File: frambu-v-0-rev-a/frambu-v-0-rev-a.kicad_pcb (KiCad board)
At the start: 2 copper layers, 50 x 60 mm, 30 parts, among them J3 Conn_02x18_Odd_Even, J4 Conn_02x18_Odd_Even, J5 USB_C_Receptacle_USB2.0_16P, SW1 PTS 636, U1 RP2040, U2 AMS1117-5.0, U3 W25Q128JVS

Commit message: nombre nuevo frambu
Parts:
- C12, C18: footprint frambuesa-rev-a:C1206 -> frambu-v-0-rev-a:C1206
- C13, C19, C20: footprint frambuesa-rev-a:C0402 -> frambu-v-0-rev-a:C0402
- J5: footprint frambuesa-rev-a:USB-C_SMD-TYPE-C-31-M-12_1 -> frambu-v-0-rev-a:USB-C_SMD-TYPE-C-31-M-12_1
- R4, R6, R7: footprint frambuesa-rev-a:R0402 -> frambu-v-0-rev-a:R0402
- SW1: footprint frambuesa-rev-a:KEY-SMD_L6.0-W3.5-LS8.7 -> frambu-v-0-rev-a:KEY-SMD_L6.0-W3.5-LS8.7
- U3: footprint frambuesa-rev-a:SOIC-8_L5.3-W5.3-P1.27-LS8.0-BL -> frambu-v-0-rev-a:SOIC-8_L5.3-W5.3-P1.27-LS8.0-BL
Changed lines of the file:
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@@
 		(property ki_fp_filters "C_*")
 		(sheetname "/")
-		(sheetfile "frambuesa-rev-a.kicad_sch")
+		(sheetfile "frambu-v-0-rev-a.kicad_sch")
 		(units
 			(unit
@@
 		(property ki_fp_filters "C_*")
 		(sheetname "/")
-		(sheetfile "frambuesa-rev-a.kicad_sch")
+		(sheetfile "frambu-v-0-rev-a.kicad_sch")
 		(units
 			(unit
@@
 		(property ki_fp_filters "C_*")
 		(sheetname "/")
-		(sheetfile "frambuesa-rev-a.kicad_sch")
+		(sheetfile "frambu-v-0-rev-a.kicad_sch")
 		(units
 			(unit
@@
 		(property ki_fp_filters "Connector*:*_2x??_*")
 		(sheetname "/")
-		(sheetfile "frambuesa-rev-a.kicad_sch")
+		(sheetfile "frambu-v-0-rev-a.kicad_sch")
 		(units
 			(unit
@@
 		(property ki_fp_filters "*QFN*7x7mm?P0.4mm?EP3.2x3.2mm*")
 		(sheetname "/")
-		(sheetfile "frambuesa-rev-a.kicad_sch")
+		(sheetfile "frambu-v-0-rev-a.kicad_sch")
 		(units
 			(unit
@@
 		)
 	)
-	(footprint "frambuesa-rev-a:KEY-SMD_L6.0-W3.5-LS8.7"
+	(footprint "frambu-v-0-rev-a:KEY-SMD_L6.0-W3.5-LS8.7"
 		(layer "F.Cu")
 		(at 82.23 44.935)
@@
 		)
 		(sheetname "/")
-		(sheetfile "frambuesa-rev-a.kicad_sch")
+		(sheetfile "frambu-v-0-rev-a.kicad_sch")
 		(units
 			(unit
@@
 		(property ki_fp_filters "C_*")
 		(sheetname "/")
-		(sheetfile "frambuesa-rev-a.kicad_sch")
+		(sheetfile "frambu-v-0-rev-a.kicad_sch")
 		(units
 			(unit
@@
 		)
 	)
-	(footprint "frambuesa-rev-a:SOIC-8_L5.3-W5.3-P1.27-LS8.0-BL"
+	(footprint "frambu-v-0-rev-a:SOIC-8_L5.3-W5.3-P1.27-LS8.0-BL"
 		(layer "F.Cu")
 		(at 72.15 70.835)
@@
 		(property ki_fp_filters "*SOIC*5.3x5.3mm*P1.27mm*")
 		(sheetname "/")
-		(sheetfile "frambuesa-rev-a.kicad_sch")
+		(sheetfile "frambu-v-0-rev-a.kicad_sch")
 		(units
 			(unit
@@
 		)
 		(embedded_fonts no)
-		(model "bibliotecas/frambuesa-rev-a.3dshapes/SOIC-8_L5.3-W5.3-H1.9-LS7.9-P1.27.wrl"
+		(model "bibliotecas/frambu-v-0-rev-a.3dshapes/SOIC-8_L5.3-W5.3-H1.9-LS7.9-P1.27.wrl"
 			(offset
 				(xyz 0 0 0)
@@
 		)
 	)
-	(footprint "frambuesa-rev-a:R0402"
+	(footprint "frambu-v-0-rev-a:R0402"
 		(layer "F.Cu")
 		(at 87.045 27.725)
@@
 		(property ki_fp_filters "R_*")
 		(sheetname "/")
-		(sheetfile "frambuesa-rev-a.kicad_sch")
+		(sheetfile "frambu-v-0-rev-a.kicad_sch")
 		(units
 			(unit
@@
 		)
 		(embedded_fonts no)
-		(model "bibliotecas/frambuesa-rev-a.3dshapes/R0402_L1.0-W0.5-H0.4.wrl"
+		(model "bibliotecas/frambu-v-0-rev-a.3dshapes/R0402_L1.0-W0.5-H0.4.wrl"
 			(offset
 				(xyz 0 0 0)
@@
 		)
 	)
-	(footprint "frambuesa-rev-a:C0402"
+	(footprint "frambu-v-0-rev-a:C0402"
 		(layer "F.Cu")
 		(at 86.655 68.905)
@@
 		(property ki_fp_filters "C_*")
 		(sheetname "/")
-		(sheetfile "frambuesa-rev-a.kicad_sch")
+		(sheetfile "frambu-v-0-rev-a.kicad_sch")
 		(units
 			(unit
@@
 		)
 		(embedded_fonts no)
-		(model "bibliotecas/frambuesa-rev-a.3dshapes/C0402_L1.0-W0.5-H0.5.wrl"
+		(model "bibliotecas/frambu-v-0-rev-a.3dshapes/C0402_L1.0-W0.5-H0.5.wrl"
 			(offset
 				(xyz 0 0 0)
@@
 		(property ki_fp_filters "C_*")
 		(sheetname "/")
-		(sheetfile "frambuesa-rev-a.kicad_sch")
+		(sheetfile "frambu-v-0-rev-a.kicad_sch")
 		(units
 			(unit
@@
 		(property ki_fp_filters "C_*")
 		(sheetname "/")
-		(sheetfile "frambuesa-rev-a.kicad_sch")
+		(sheetfile "frambu-v-0-rev-a.kicad_sch")
 		(units
 			(unit
@@
 		)
 	)
-	(footprint "frambuesa-rev-a:R0402"
+	(footprint "frambu-v-0-rev-a:R0402"
 		(layer "F.Cu")
 		(at 87.045 25.575)
@@
 		(property ki_fp_filters "R_*")
 		(sheetname "/")
-		(sheetfile "frambuesa-rev-a.kicad_sch")
+		(sheetfile "frambu-v-0-rev-a.kicad_sch")
 		(units
 			(unit
@@
 		)
 		(embedded_fonts no)
-		(model "bibliotecas/frambuesa-rev-a.3dshapes/R0402_L1.0-W0.5-H0.4.wrl"
+		(model "bibliotecas/frambu-v-0-rev-a.3dshapes/R0402_L1.0-W0.5-H0.4.wrl"
 			(offset
 				(xyz 0 0 0)
@@
 		)
 	)
-	(footprint "frambuesa-rev-a:C0402"
+	(footprint "frambu-v-0-rev-a:C0402"
 		(layer "F.Cu")
 		(at 86.655 66.755)
@@
 		(property ki_fp_filters "C_*")
 		(sheetname "/")
-		(sheetfile "frambuesa-rev-a.kicad_sch")
+		(sheetfile "frambu-v-0-rev-a.kicad_sch")
 		(units
 			(unit
@@
 		)
 		(embedded_fonts no)
-		(model "bibliotecas/frambuesa-rev-a.3dshapes/C0402_L1.0-W0.5-H0.5.wrl"
+		(model "bibliotecas/frambu-v-0-rev-a.3dshapes/C0402_L1.0-W0.5-H0.5.wrl"
 			(offset
 				(xyz 0 0 0)
@@
 		(property ki_fp_filters "C_*")
 		(sheetname "/")
-		(sheetfile "frambuesa-rev-a.kicad_sch")
+		(sheetfile "frambu-v-0-rev-a.kicad_sch")
 		(units
 			(unit
@@
 		(property ki_fp_filters "C_*")
 		(sheetname "/")
-		(sheetfile "frambuesa-rev-a.kicad_sch")
+		(sheetfile "frambu-v-0-rev-a.kicad_sch")
 		(units
 			(unit
@@
 		(property ki_fp_filters "C_*")
 		(sheetname "/")
-		(sheetfile "frambuesa-rev-a.kicad_sch")
+		(sheetfile "frambu-v-0-rev-a.kicad_sch")
 		(units
 			(unit
@@
 		(property ki_fp_filters "SOT?223*TabPin2*")
 		(sheetname "/")
-		(sheetfile "frambuesa-rev-a.kicad_sch")
+		(sheetfile "frambu-v-0-rev-a.kicad_sch")
 		(units
 			(unit
@@
 		(property ki_fp_filters "R_*")
 		(sheetname "/")
-		(sheetfile "frambuesa-rev-a.kicad_sch")
+		(sheetfile "frambu-v-0-rev-a.kicad_sch")
 		(units
 			(unit
@@
 		)
 	)
-	(footprint "frambuesa-rev-a:USB-C_SMD-TYPE-C-31-M-12_1"
+	(footprint "frambu-v-0-rev-a:USB-C_SMD-TYPE-C-31-M-12_1"
 		(layer "F.Cu")
 		(at 74.11 59.970088)
@@
 		(property ki_fp_filters "USB*C*Receptacle*")
 		(sheetname "/")
-		(sheetfile "frambuesa-rev-a.kicad_sch")
+		(sheetfile "frambu-v-0-rev-a.kicad_sch")
 		(units
 			(unit
@@
 		)
 		(embedded_fonts no)
-		(model "bibliotecas/frambuesa-rev-a.3dshapes/USB-C_SMD-TYPE-C-31-M-12_1.wrl"
+		(model "bibliotecas/frambu-v-0-rev-a.3dshapes/USB-C_SMD-TYPE-C-31-M-12_1.wrl"
 			(offset
 				(xyz 0 0 0)
@@
 		(property ki_fp_filters "C_*")
 		(sheetname "/")
-		(sheetfile "frambuesa-rev-a.kicad_sch")
+		(sheetfile "frambu-v-0-rev-a.kicad_sch")
 		(units
 			(unit
@@
 		)
 	)
-	(footprint "frambuesa-rev-a:C1206"
+	(footprint "frambu-v-0-rev-a:C1206"
 		(layer "F.Cu")
 		(at 87.515 52.305)
@@
 		(property ki_fp_filters "C_*")
 		(sheetname "/")
-		(sheetfile "frambuesa-rev-a.kicad_sch")
+		(sheetfile "frambu-v-0-rev-a.kicad_sch")
 		(units
 			(unit
@@
 		)
 		(embedded_fonts no)
-		(model "bibliotecas/frambuesa-rev-a.3dshapes/C1206_L3.2-W1.6-H1.3.wrl"
+		(model "bibliotecas/frambu-v-0-rev-a.3dshapes/C1206_L3.2-W1.6-H1.3.wrl"
 			(offset
 				(xyz 0 0 0)
@@
 		(property ki_fp_filters "R_*")
 		(sheetname "/")
-		(sheetfile "frambuesa-rev-a.kicad_sch")
+		(sheetfile "frambu-v-0-rev-a.kicad_sch")
 		(units
 			(unit
@@
 		(property ki_fp_filters "C_*")
 		(sheetname "/")
-		(sheetfile "frambuesa-rev-a.kicad_sch")
+		(sheetfile "frambu-v-0-rev-a.kicad_sch")
 		(units
 			(unit
@@
 		)
 	)
-	(footprint "frambuesa-rev-a:R0402"
+	(footprint "frambu-v-0-rev-a:R0402"
 		(layer "F.Cu")
 		(at 87.045 29.875)
@@
 		(property ki_fp_filters "R_*")
 		(sheetname "/")
-		(sheetfile "frambuesa-rev-a.kicad_sch")
+		(sheetfile "frambu-v-0-rev-a.kicad_sch")
 		(units
 			(unit
@@
 		)
 		(embedded_fonts no)
-		(model "bibliotecas/frambuesa-rev-a.3dshapes/R0402_L1.0-W0.5-H0.4.wrl"
+		(model "bibliotecas/frambu-v-0-rev-a.3dshapes/R0402_L1.0-W0.5-H0.4.wrl"
 			(offset
 				(xyz 0 0 0)
@@
 		(property ki_fp_filters "C_*")
 		(sheetname "/")
-		(sheetfile "frambuesa-rev-a.kicad_sch")
+		(sheetfile "frambu-v-0-rev-a.kicad_sch")
 		(units
 			(unit
@@
 		)
 	)
-	(footprint "frambuesa-rev-a:C0402"
+	(footprint "frambu-v-0-rev-a:C0402"
 		(layer "F.Cu")
 		(at 86.655 71.055)
@@
 		(property ki_fp_filters "C_*")
 		(sheetname "/")
-		(sheetfile "frambuesa-rev-a.kicad_sch")
+		(sheetfile "frambu-v-0-rev-a.kicad_sch")
 		(units
 			(unit
@@
 		)
 		(embedded_fonts no)
-		(model "bibliotecas/frambuesa-rev-a.3dshapes/C0402_L1.0-W0.5-H0.5.wrl"
+		(model "bibliotecas/frambu-v-0-rev-a.3dshapes/C0402_L1.0-W0.5-H0.5.wrl"
 			(offset
 				(xyz 0 0 0)
@@
 		(property ki_fp_filters "Connector*:*_2x??_*")
 		(sheetname "/")
-		(sheetfile "frambuesa-rev-a.kicad_sch")
+		(sheetfile "frambu-v-0-rev-a.kicad_sch")
 		(units
 			(unit
@@
 		)
 	)
-	(footprint "frambuesa-rev-a:C1206"
+	(footprint "frambu-v-0-rev-a:C1206"
 		(layer "F.Cu")
 		(at 87.515 48.975)
@@
 		(property ki_fp_filters "C_*")
 		(sheetname "/")
-		(sheetfile "frambuesa-rev-a.kicad_sch")
+		(sheetfile "frambu-v-0-rev-a.kicad_sch")
 		(units
 			(unit
@@
 		)
 		(embedded_fonts no)
-		(model "bibliotecas/frambuesa-rev-a.3dshapes/C1206_L3.2-W1.6-H1.3.wrl"
+		(model "bibliotecas/frambu-v-0-rev-a.3dshapes/C1206_L3.2-W1.6-H1.3.wrl"
 			(offset
 				(xyz 0 0 0)
@@
 		(property ki_fp_filters "MountingHole*")
 		(sheetname "/")
-		(sheetfile "frambuesa-rev-a.kicad_sch")
+		(sheetfile "frambu-v-0-rev-a.kicad_sch")
 		(units
 			(unit

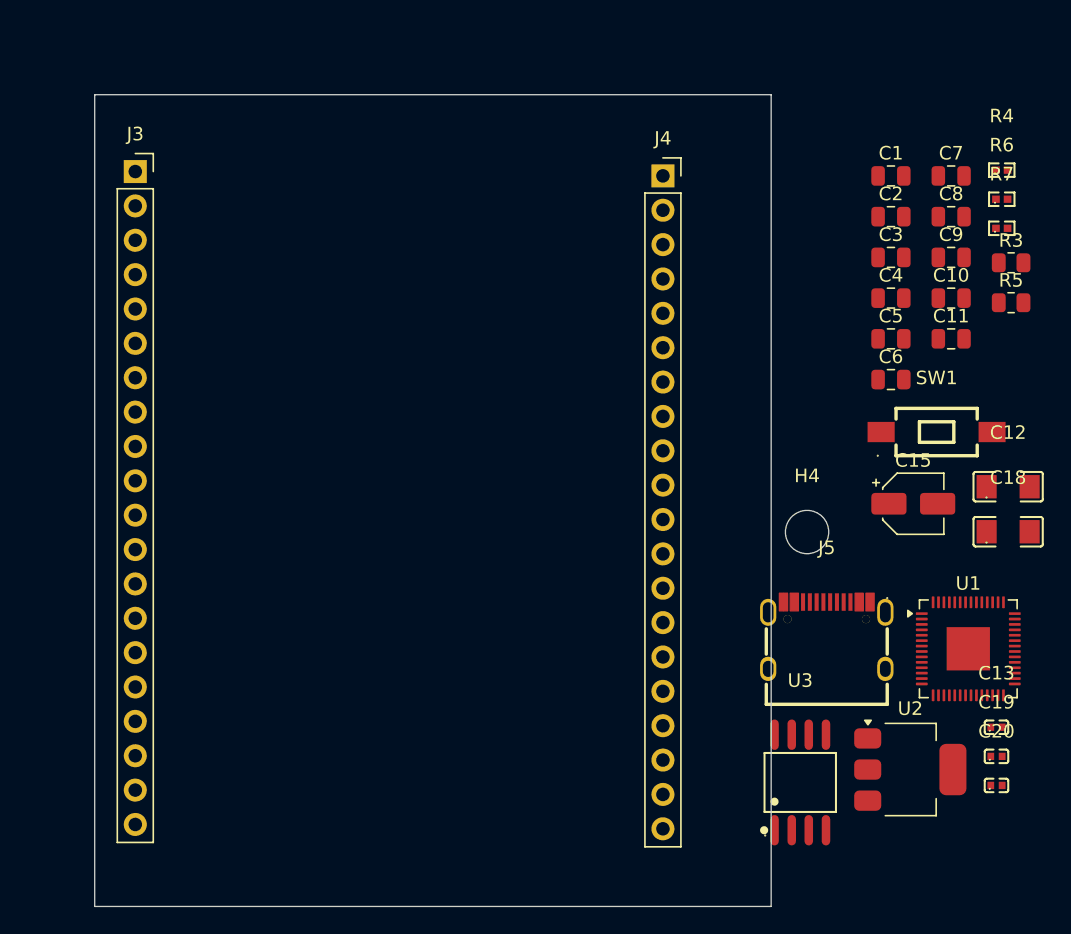
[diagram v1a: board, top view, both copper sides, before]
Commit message: agregar version de pcb
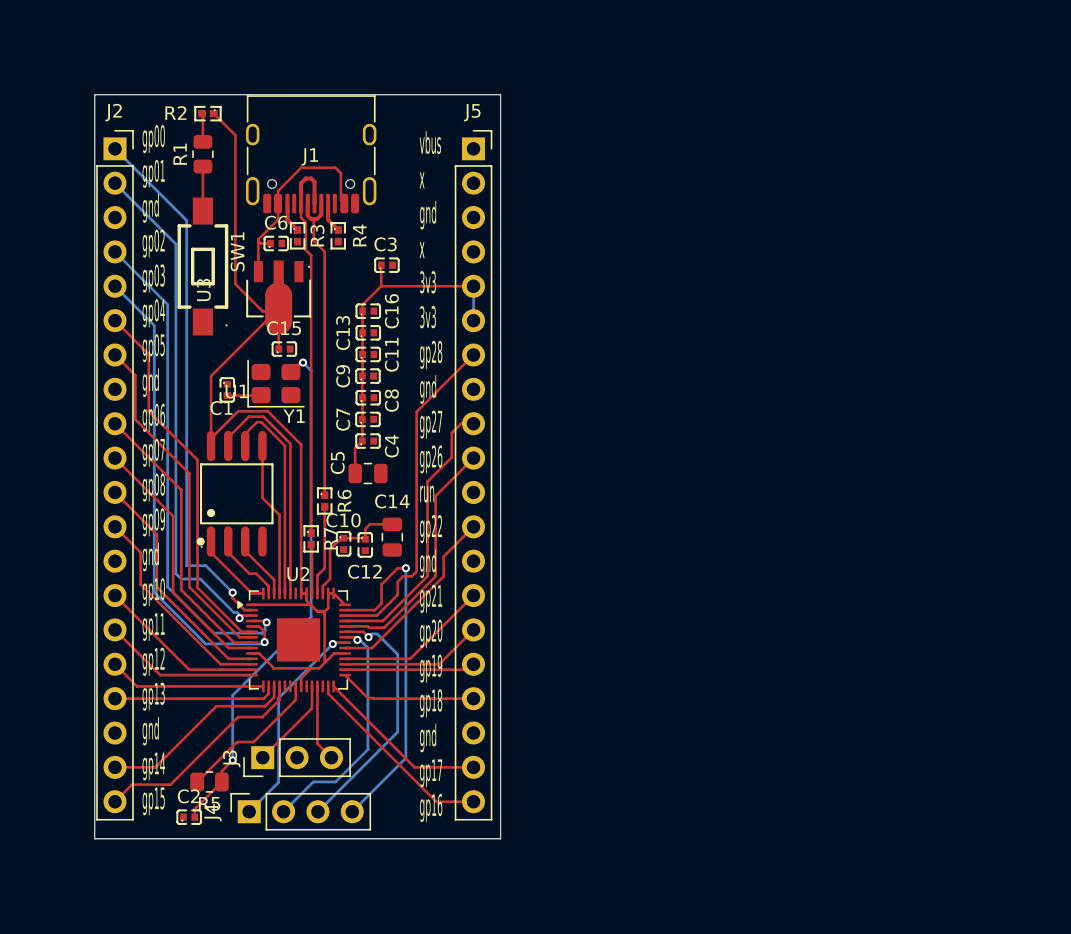
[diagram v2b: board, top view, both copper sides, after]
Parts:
- removed C18: 100u, frambu-v-0-rev-a:C1206
- removed C19, C20: 10u, frambu-v-0-rev-a:C0402
- removed H4: MountingHole, MountingHole:MountingHole_3.2mm_M3
- added C14: 1u, Capacitor_SMD:C_0805_2012Metric, F.Cu at (42.0, 52.7)
- added C16: 100n, frambu-v-0-rev-a:C0402, F.Cu at (40.2, 36.0)
- added J1: USB_C_Receptacle_USB2.0_16P, Connector_USB:USB_C_Receptacle_HRO_TYPE-C-31-M-12, F.Cu at (36.0, 24.0)
- added J2: pico_pines_1-20, Connector_PinSocket_2.54mm:PinSocket_1x20_P2.54mm_Vertical, F.Cu at (21.5, 24.0)
- added R1: 1k, Resistor_SMD:R_0805_2012Metric, F.Cu at (28.0, 24.4)
- added R2: 10k, frambu-v-0-rev-a:R0402, F.Cu at (28.4, 21.4)
- added Y1: 12MHz, Crystal:Crystal_SMD_3225-4Pin_3.2x2.5mm, F.Cu at (33.4, 41.4)
- C1: value 1u -> 15p; footprint Capacitor_SMD:C_0805_2012Metric -> frambu-v-0-rev-a:C0402
- C10, C11, C4, C7, C8: footprint Capacitor_SMD:C_0805_2012Metric -> frambu-v-0-rev-a:C0402
- C12: value 100u -> 100n; footprint frambu-v-0-rev-a:C1206 -> frambu-v-0-rev-a:C0402
- C13: value 10u -> 100n
- C15: footprint Capacitor_SMD:CP_Elec_4x5.4 -> frambu-v-0-rev-a:C0402
- C2: value 100n -> 15p; footprint Capacitor_SMD:C_0805_2012Metric -> frambu-v-0-rev-a:C0402
- C3, C6: value 100n -> 10u; footprint Capacitor_SMD:C_0805_2012Metric -> frambu-v-0-rev-a:C0402
- C5: value 100n -> 1u
- C9: value 1u -> 100n; footprint Capacitor_SMD:C_0805_2012Metric -> frambu-v-0-rev-a:C0402
- J3: value Conn_02x18_Odd_Even -> SWD; footprint Connector_PinSocket_2.54mm:PinSocket_1x20_P2.54mm_Vertical -> Connector_PinHeader_2.54mm:PinHeader_1x03_P2.54mm_Vertical
- J4: value Conn_02x18_Odd_Even -> GPIO_extra; footprint Connector_PinSocket_2.54mm:PinSocket_1x20_P2.54mm_Vertical -> Connector_PinSocket_2.54mm:PinSocket_1x04_P2.54mm_Vertical
- J5: value USB_C_Receptacle_USB2.0_16P -> pico_pines_40-21; footprint frambu-v-0-rev-a:USB-C_SMD-TYPE-C-31-M-12_1 -> Connector_PinSocket_2.54mm:PinSocket_1x20_P2.54mm_Vertical
- R3: value 1k -> 5k1; footprint Resistor_SMD:R_0805_2012Metric -> frambu-v-0-rev-a:R0402
- R4: value 10k -> 5k1
- R5: value 1K -> 1k
- R6, R7: value 5k1 -> 27
- U1: value RP2040 -> W25Q128JVS; footprint Package_DFN_QFN:QFN-56-1EP_7x7mm_P0.4mm_EP3.2x3.2mm -> frambu-v-0-rev-a:SOIC-8_L5.3-W5.3-P1.27-LS8.0-BL
- U2: value AMS1117-5.0 -> RP2040; footprint Package_TO_SOT_SMD:SOT-223-3_TabPin2 -> Package_DFN_QFN:QFN-56-1EP_7x7mm_P0.4mm_EP3.2x3.2mm
- U3: value W25Q128JVS -> AMS1117-3.3; footprint frambu-v-0-rev-a:SOIC-8_L5.3-W5.3-P1.27-LS8.0-BL -> frambu-v-0-rev-a:SOT-89-3_L4.5-W2.5-P1.50-LS4.2-BR
- moved R5 69.0 mm to (28.5, 70.8), turned to 180 degrees
- moved C2 68.3 mm to (27.0, 73.4)
- moved J4 56.1 mm to (31.4, 73.0), turned to 90 degrees
- moved R7 56.0 mm to (36.0, 52.8), turned to -90 degrees
- moved SW1 55.6 mm to (28.0, 32.7), turned to 90 degrees
- moved U1 55.3 mm to (30.5, 49.5)
- moved C13 54.8 mm to (40.2, 37.6)
- moved R6 54.8 mm to (37.0, 50.0), turned to -90 degrees
- moved U3 53.0 mm to (33.6, 34.4), turned to 90 degrees
- moved R3 52.8 mm to (35.0, 30.4), turned to -90 degrees
- moved C1 51.5 mm to (29.8, 41.8), turned to -90 degrees
- moved R4 49.3 mm to (38.0, 30.4), turned to -90 degrees
- moved C10 48.4 mm to (38.4, 53.2), turned to -90 degrees
- moved C15 47.9 mm to (34.0, 38.8)
- moved C12 47.7 mm to (40.0, 53.3), turned to -90 degrees
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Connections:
- C1 pad 1: +3V3 -> GND
- C1 pad 2: GND -> /XIN
- C11 pad 1: +1V1 -> +3V3
- C12 pad 1: VHI -> +1V1
- C13 pad 1: VHI -> +3V3
- C2 pad 1: +3V3 -> GND
- C2 pad 2: GND -> Net-(C2-Pad2)
- C6 pad 1: +3V3 -> VBUS
- C9 pad 1: +1V1 -> +3V3
- J3 pad 1: GND -> /SWCLK
- J3 pad 2: +3V3 -> GND
- J3 pad 3: GND -> /SWD
- J4 pad 1: /GPIO29_ADC3 -> /GPIO23
- J4 pad 2: GND -> /GPIO24
- J4 pad 3: /GPIO28_ADC2 -> /GPIO25
- J4 pad 4: GND -> /GPIO29_ADC3
- J5 pad 1: (no net) -> VBUS
- J5 pad 2: (no net) -> unconnected-(J5-Pin_2-Pad2)
- J5 pad 3: (no net) -> GND
- J5 pad 4: (no net) -> unconnected-(J5-Pin_4-Pad4)
- R3 pad 1: Net-(SW1-B) -> Net-(J1-CC2)
- R3 pad 2: /QSPI_SS -> GND
- R4 pad 1: +3V3 -> Net-(J1-CC1)
- R4 pad 2: /QSPI_SS -> GND
- R5 pad 1: Net-(C17-Pad2) -> Net-(C2-Pad2)
- R6 pad 1: Net-(J5-CC1) -> /USB_D-
- R6 pad 2: GND -> Net-(U2-USB_DM)
- R7 pad 1: Net-(J5-CC2) -> /USB_D+
- R7 pad 2: GND -> Net-(U2-USB_DP)
- U1 pad 1: +3V3 -> /QSPI_SS
- U1 pad 2: /GPIO00 -> /QSPI_SD1
- U1 pad 3: /GPIO01 -> /QSPI_SD2
- U1 pad 4: /GPIO02 -> GND
- U1 pad 5: /GPIO03 -> /QSPI_SD0
- U1 pad 6: /GPIO04 -> /QSPI_SCLK
- U1 pad 7: /GPIO05 -> /QSPI_SD3
- U1 pad 8: /GPIO06 -> +3V3
- U2 pad 1: GND -> +3V3
- U2 pad 2: +3.3V -> /GPIO00
- U2 pad 3: VHI -> /GPIO01
- U3 pad 1: /QSPI_SS -> GND
- U3 pad 2: /QSPI_SD1 -> +3V3
- U3 pad 3: /QSPI_SD2 -> VBUS
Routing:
- net +3V3: track 0.00 -> 102.0 mm
- net /GPIO00: track 0.00 -> 39.4 mm, vias 0 -> 1
- net Net-(C2-Pad2): track 0.00 -> 38.7 mm, vias 0 -> 2
- net /GPIO01: track 0.00 -> 38.0 mm, vias 0 -> 1
- net /GPIO02: track 0.00 -> 36.9 mm, vias 0 -> 1
- net /GPIO03: track 0.00 -> 35.5 mm, vias 0 -> 1
- net /USB_D+: track 0.00 -> 29.0 mm
- net /GPIO04: track 0.00 -> 27.6 mm
- net /GPIO29_ADC3: track 0.00 -> 26.2 mm, vias 0 -> 1
- net /GPIO05: track 0.00 -> 25.6 mm
- net /GPIO28_ADC2: track 0.00 -> 25.0 mm
- net /USB_D-: track 0.00 -> 23.7 mm
- net /GPIO06: track 0.00 -> 21.2 mm
- net /GPIO27_ADC1: track 0.00 -> 20.7 mm
- net /GPIO07: track 0.00 -> 19.2 mm
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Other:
- board size 50 x 60 mm -> 30 x 55 mm
- board text added: "gp00 gp01 gnd gp02 gp03 gp04 gp05 gnd gp06 gp07 gp08 gp09 gnd gp10 gp11 gp12 gp13 gnd gp14 gp15"
- board text added: "vbus x gnd x 3v3 3v3 gp28 gnd gp27 gp26 run gp22 gnd gp21 gp20 gp19 gp18 gnd gp17 gp16"

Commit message: agregar pcb
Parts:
- removed C16, C4, C7, C8: 100n, frambu-v-0-rev-a:C0402
- removed J3: SWD, Connector_PinHeader_2.54mm:PinHeader_1x03_P2.54mm_Vertical
- removed J4: GPIO_extra, Connector_PinSocket_2.54mm:PinSocket_1x04_P2.54mm_Vertical
- moved C13 19.8 mm to (50.5, 54.5)
- moved R5 18.3 mm to (41.8, 58.2), turned to 90 degrees
- moved Y1 18.1 mm to (38.5, 58.8), turned to 180 degrees
- moved C1 17.9 mm to (35.8, 58.8), turned to 90 degrees
- moved R7 17.3 mm to (43.2, 37.1)
- moved R6 17.2 mm to (43.2, 34.0)
- moved R2 17.1 mm to (29.8, 38.4), turned to 90 degrees
- moved C2 16.2 mm to (39.0, 62.5), turned to 180 degrees
- moved U3 15.1 mm to (48.2, 31.0)
- moved C3 14.4 mm to (46.2, 46.2)
- moved C6 13.9 mm to (46.8, 26.9), turned to 90 degrees
- moved C11 12.7 mm to (27.7, 37.0), turned to 90 degrees
- moved U1 11.9 mm to (34.5, 38.2)
- moved C15 11.9 mm to (44.0, 45.2)
- moved U2 11.7 mm to (39.7, 49.5)
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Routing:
- net Net-(C2-Pad2): track 38.7 -> 8.10 mm, vias 2 -> 0
- net GND: track 0.00 -> 29.0 mm, vias 0 -> 3
- net /GPIO29_ADC3: track 26.2 -> 0.00 mm, vias 1 -> 0
- net +1V1: track 9.36 -> 32.9 mm, vias 0 -> 4
- net /QSPI_SS: track 8.04 -> 31.6 mm
- net /RUN: track 0.00 -> 20.8 mm, vias 0 -> 2
- net /GPIO25: track 18.9 -> 0.00 mm, vias 1 -> 0
- net /GPIO24: track 17.8 -> 0.00 mm, vias 1 -> 0
- net VBUS: track 15.4 -> 31.3 mm
- net /GPIO23: track 15.9 -> 0.00 mm, vias 1 -> 0
- net /USB_D-: track 23.7 -> 10.1 mm
- net /GPIO02: track 36.9 -> 23.7 mm, vias 1 -> 0
- net /USB_D+: track 29.0 -> 16.0 mm
- net /GPIO03: track 35.5 -> 22.7 mm, vias 1 -> 0
- net /GPIO16: track 14.6 -> 26.2 mm
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- added copper zone on B.Cu, net GND
- added copper zone on F.Cu, net GND
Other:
- board size 30 x 55 mm -> 40 x 55 mm
- board text added: "2026-10"
- board text added: "frambu"
- board text added: "v-0 rev-a"

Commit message: agregar nueva version frambu
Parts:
- added C4: 100n, frambu-v-0-rev-a:C0402, F.Cu at (52.4, 30.5)
- added C7: 100n, frambu-v-0-rev-a:C0402, F.Cu at (32.2, 46.1)
- added C8: 100n, frambu-v-0-rev-a:C0402, F.Cu at (41.1, 41.5)
- added J3: SWD, Connector_PinHeader_2.54mm:PinHeader_1x03_P2.54mm_Vertical, F.Cu at (37.5, 68.0)
- moved C14 3.00 mm to (40.5, 38.2)
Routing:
- net +1V1: track 32.9 -> 53.1 mm, vias 4 -> 5
- net /SWCLK: track 0.00 -> 18.0 mm, vias 0 -> 2
- net /SWD: track 0.00 -> 15.9 mm, vias 0 -> 2
- net +3V3: track 92.0 -> 103.6 mm
- net /GPIO00: track 29.9 -> 34.1 mm
- net /RUN: track 20.8 -> 21.7 mm
- net /GPIO04: track 19.8 -> 20.7 mm, vias 0 -> 1
- net /GPIO02: track 23.7 -> 24.5 mm, vias 0 -> 1
- net /GPIO01: track 28.2 -> 28.8 mm, vias 0 -> 1
- net /GPIO03: vias 0 -> 1
- net GND: vias 3 -> 19
